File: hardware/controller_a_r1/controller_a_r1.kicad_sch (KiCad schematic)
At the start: 15 parts, among them J101 Front Connector, U102 STM32G071KBU6

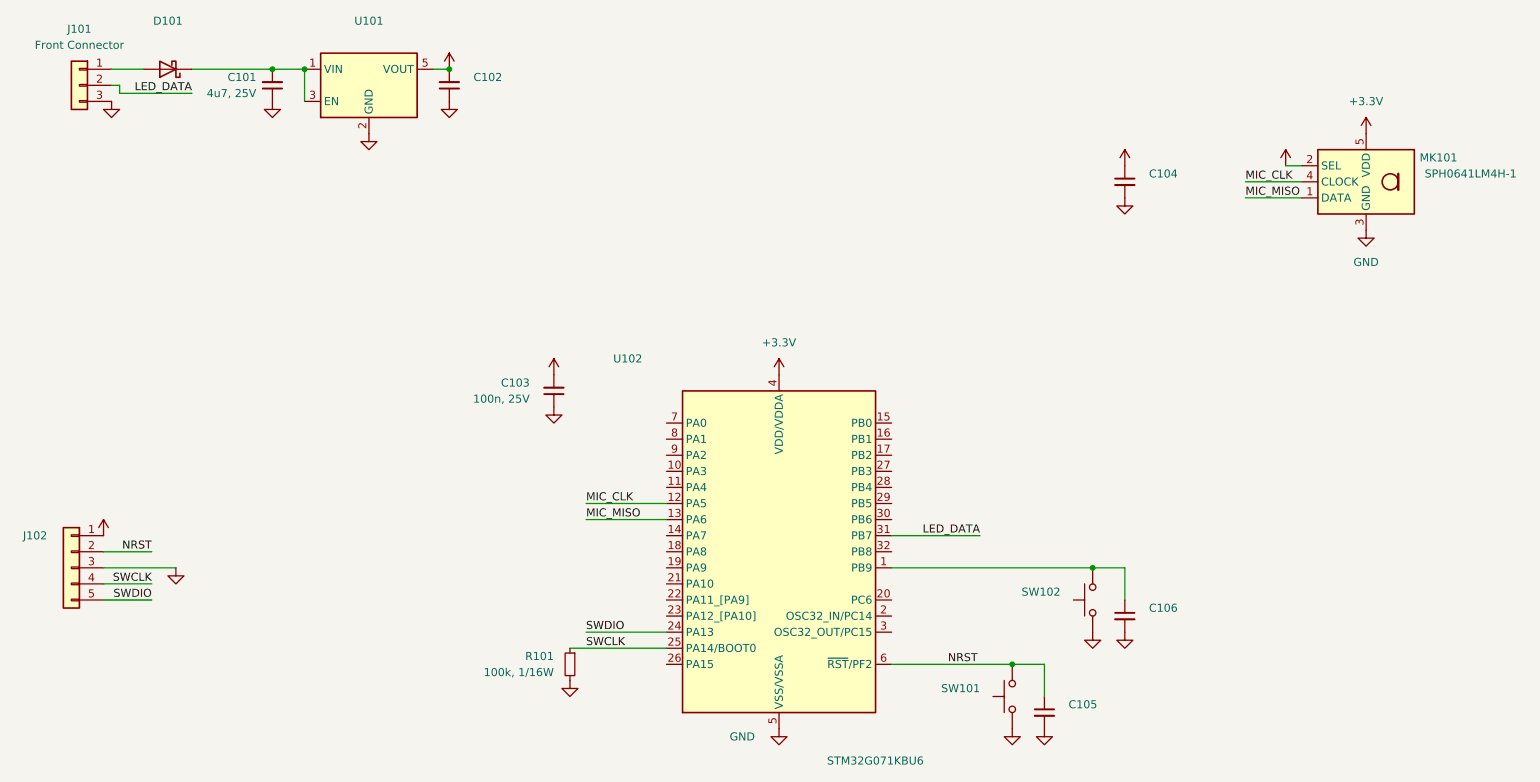
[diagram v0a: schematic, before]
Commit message: Updated kicad files to work with latest kicad. Added some todos for next hw design.
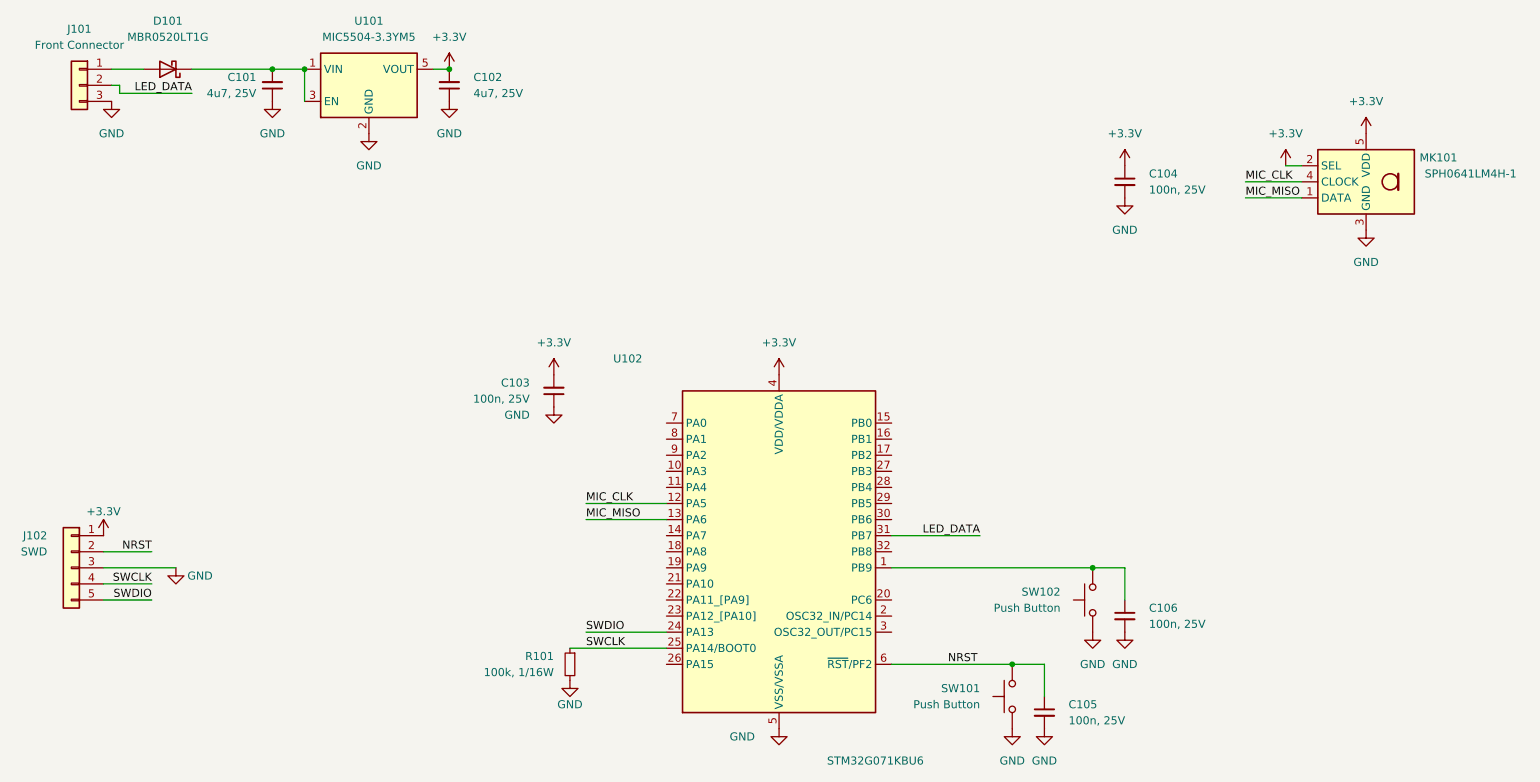
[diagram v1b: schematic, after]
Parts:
- C102: value (none) -> 4u7, 25V
- C104, C105, C106: value (none) -> 100n, 25V
- D101: value (none) -> MBR0520LT1G
- J102: value (none) -> SWD
- SW101, SW102: value (none) -> Push Button
- U101: value (none) -> MIC5504-3.3YM5
